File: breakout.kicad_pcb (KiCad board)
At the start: 2 copper layers, 103 x 62 mm, 32 parts, among them CON1 SD_Card, CON2 USB-MICRO-AB, P2 CONN_01X40, P3 CONN_01X40, P4 CONN_01X40, P5 A-DF-09-A/KG-T4S, SW1 SW_PUSH

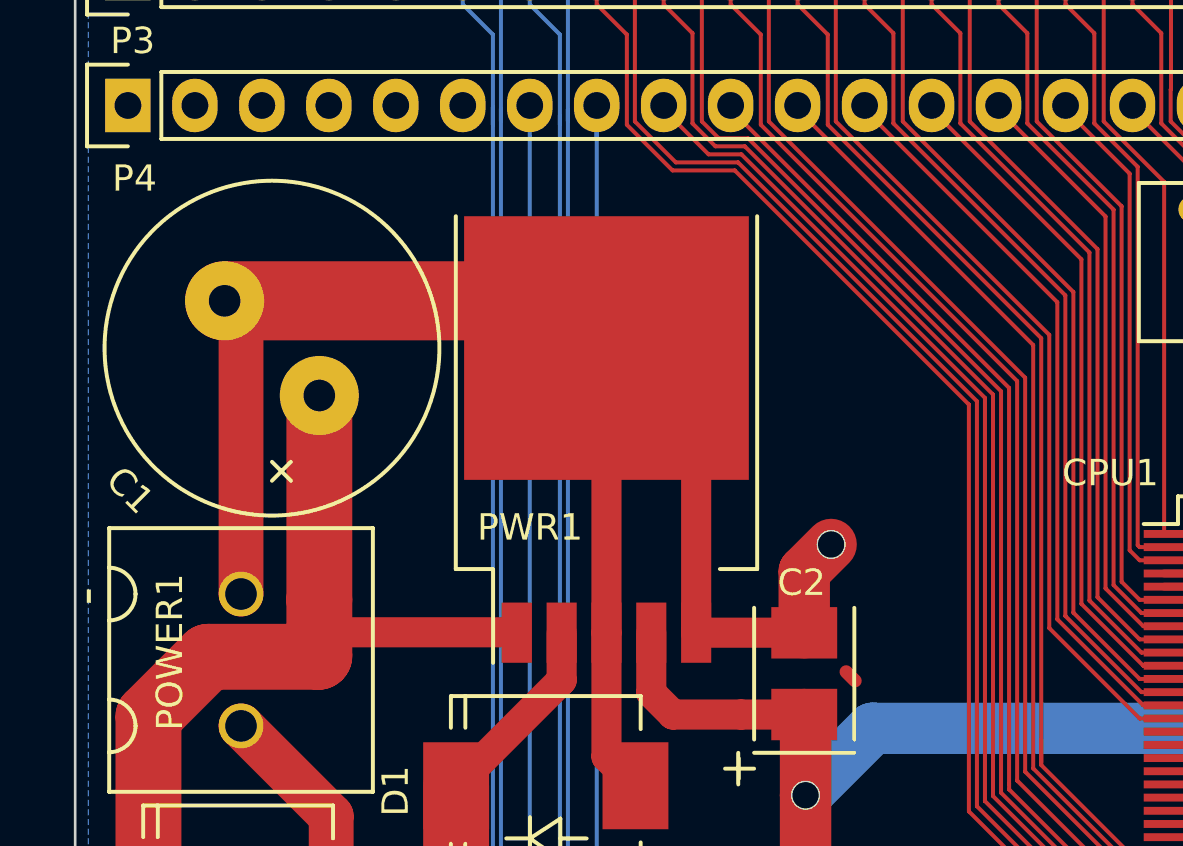
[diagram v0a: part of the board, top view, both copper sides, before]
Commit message: added thermal sink for 3.3reg
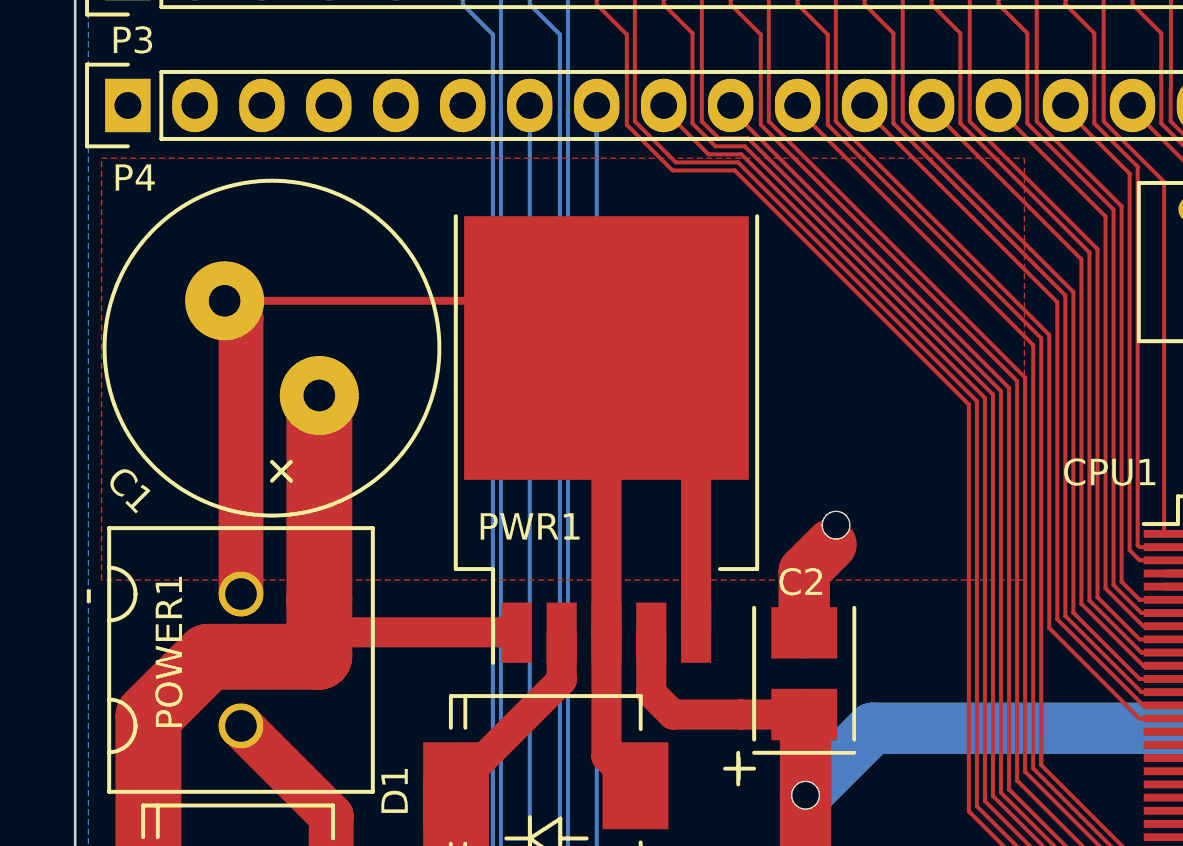
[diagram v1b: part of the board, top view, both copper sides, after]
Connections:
- P2 pad 25: (no net) -> GND
- P2 pad 26: (no net) -> GND
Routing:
- net GND: track 143.9 -> 139.8 mm

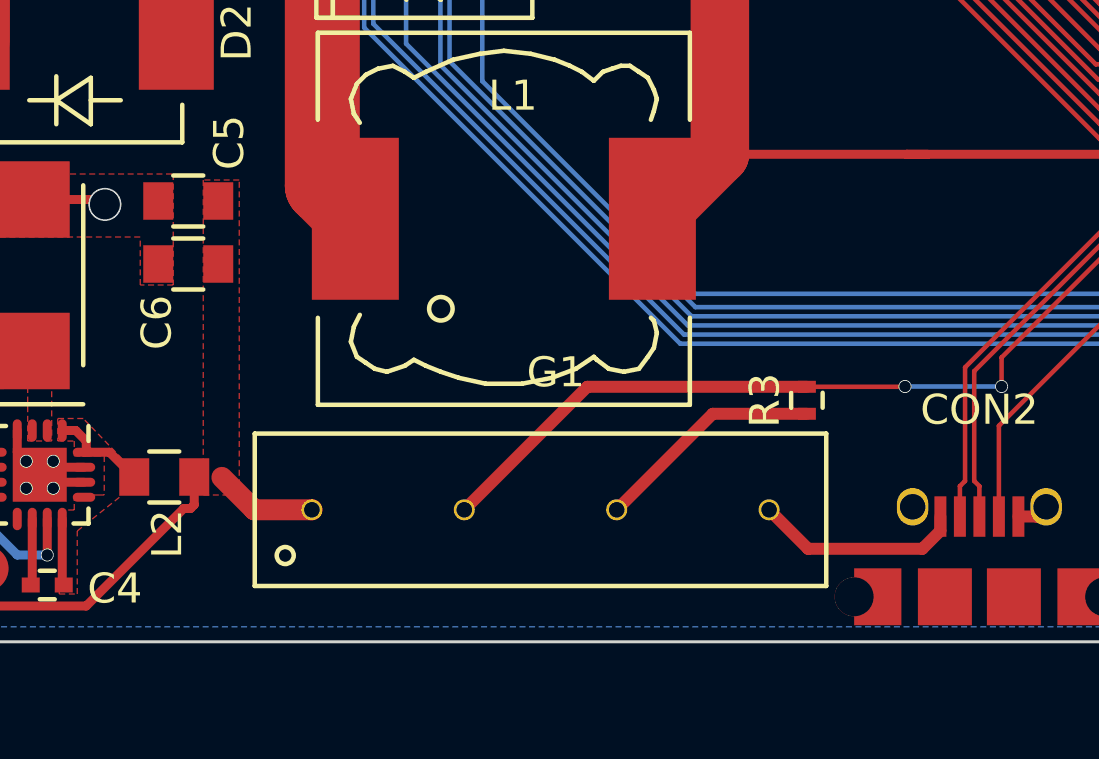
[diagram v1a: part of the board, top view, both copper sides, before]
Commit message: improved 5V FET and added to schematic & board
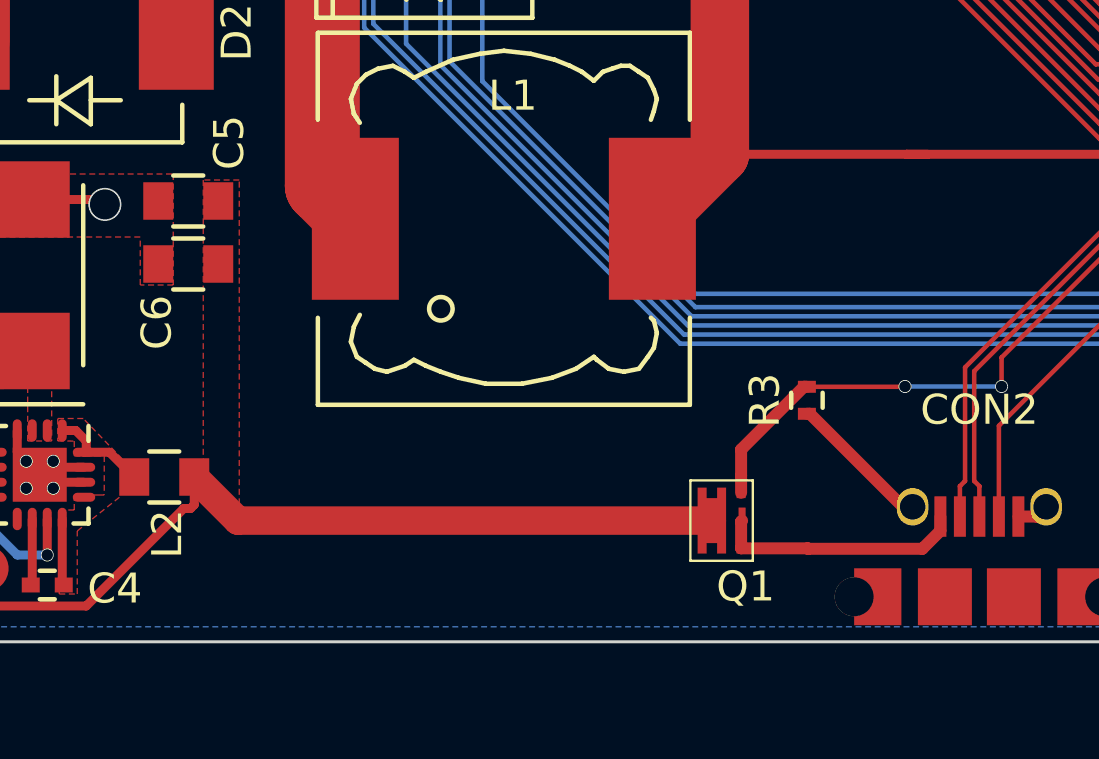
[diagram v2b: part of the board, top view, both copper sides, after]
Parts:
- removed G1: 9007-05-00, Custom Footprints:9007-05-00
- added Q1: SIA461DJ-T1-GE3, Custom Footprints:PowerPak_SC-70-6L-Single, F.Cu at (85.8, 171.0)
- CON1: footprint SD_MMC_Card_Receptacle -> Custom Footprints:SD_MMC_Card_Receptacle
- CON2: footprint USB_MICRO_AB -> Custom Footprints:USB_MICRO_AB
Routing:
- net /5V: track 19.8 -> 34.2 mm
- net /USB0_PPWR: track 36.9 -> 28.3 mm
- net GND: track 139.8 -> 136.9 mm
- net Net-(CON2-Pad1): track 6.97 -> 8.31 mm

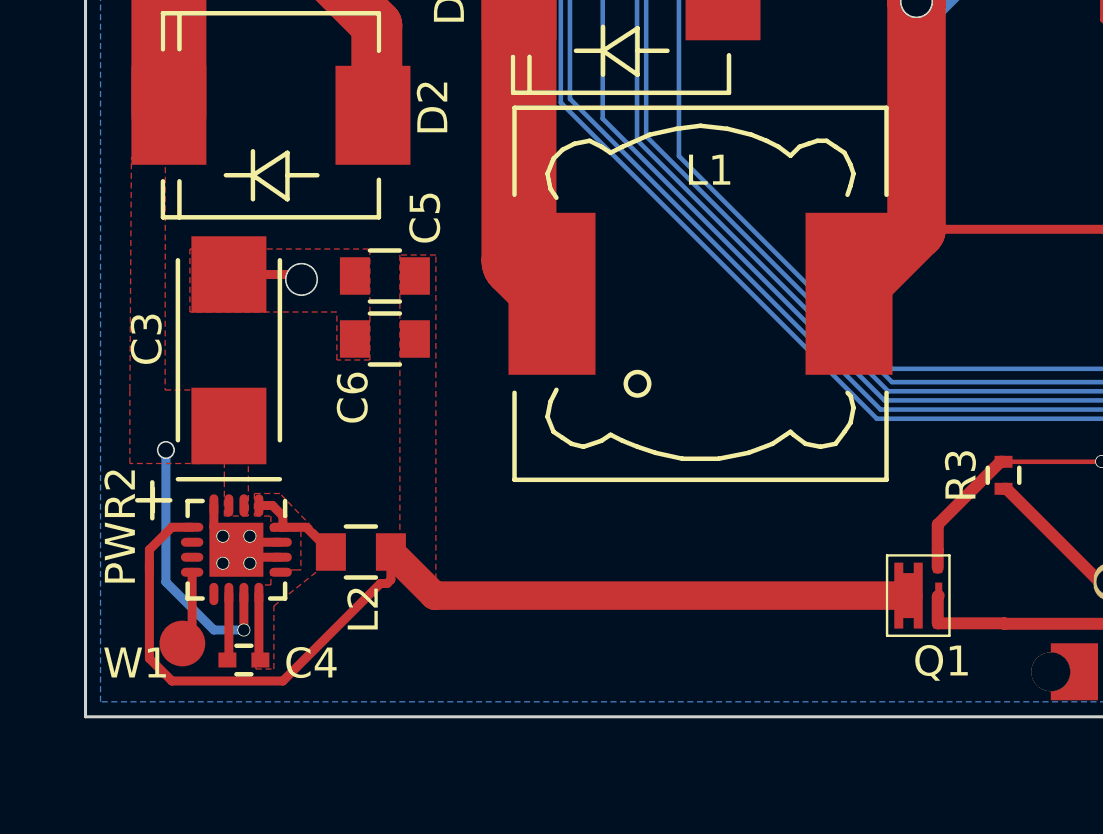
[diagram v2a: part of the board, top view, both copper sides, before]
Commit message: routed 5V FET
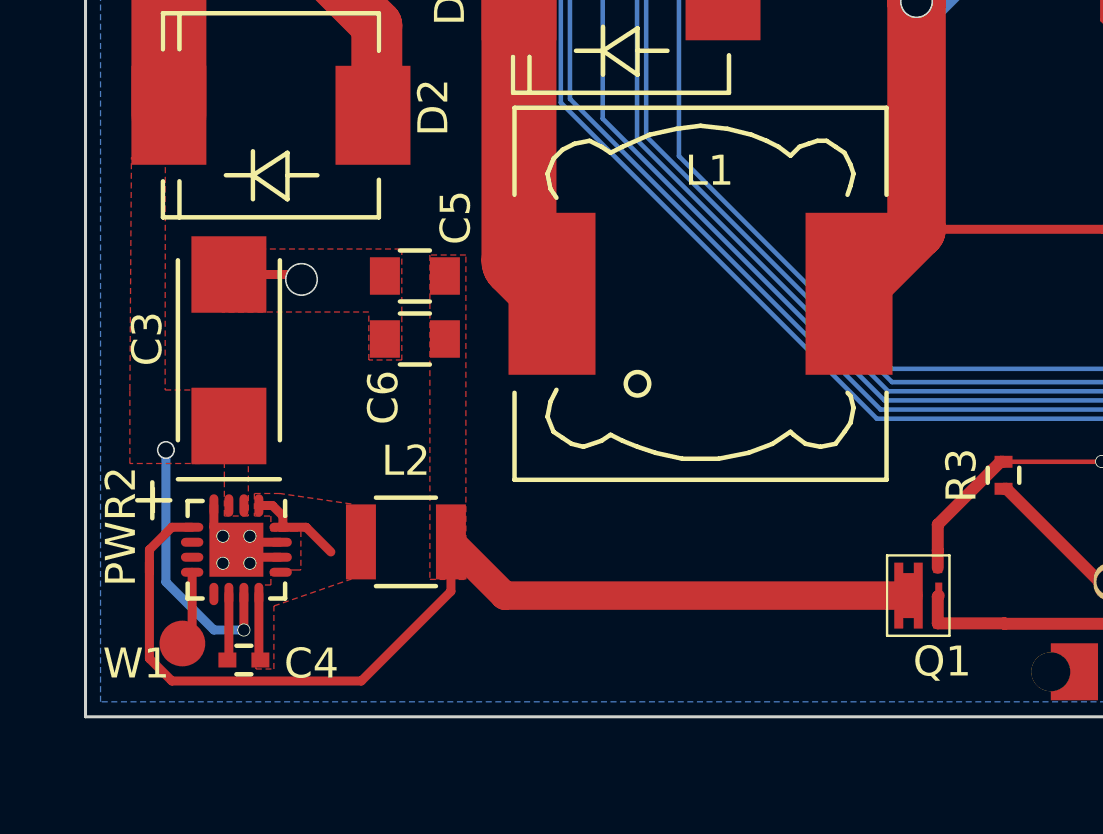
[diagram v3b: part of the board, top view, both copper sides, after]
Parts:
- L2: footprint Capacitors_SMD:C_0805 -> Capacitors_SMD:C_1210
- moved L2 1.54 mm to (68.7, 169.2)
- moved C5 1.00 mm to (69.0, 160.3)
- moved C6 1.00 mm to (69.0, 162.4)
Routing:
- net /5V: track 34.2 -> 34.9 mm
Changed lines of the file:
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@@
   (general
     (links 229)
-    (no_connects 22)
+    (no_connects 50)
     (area 57.949999 112.949999 161.050001 175.050001)
     (thickness 1.6)
     (drawings 11)
-    (tracks 1089)
+    (tracks 1087)
     (zones 0)
     (modules 32)
@@
       (net 1 GND))
   )
-  (module Capacitors_SMD:C_0805 locked (layer F.Cu)
-    (at 67.1787 169.50688)
-    (descr "Capacitor SMD 0805, reflow soldering, AVX (see smccp.pdf)")
-    (tags "capacitor 0805")
-    (attr smd)
-    (fp_text reference L2 (at 0.1 1.9 90) (layer F.SilkS)
-      (effects (font (size 1 1) (thickness 0.15)))
-    )
-    (fp_text value 4.7uH (at 0 2.1) (layer F.Fab)
-      (effects (font (size 1 1) (thickness 0.15)))
-    )
-    (fp_line (start -1.8 -1) (end 1.8 -1) (layer F.CrtYd) (width 0.05))
-    (fp_line (start -1.8 1) (end 1.8 1) (layer F.CrtYd) (width 0.05))
-    (fp_line (start -1.8 -1) (end -1.8 1) (layer F.CrtYd) (width 0.05))
-    (fp_line (start 1.8 -1) (end 1.8 1) (layer F.CrtYd) (width 0.05))
-    (fp_line (start 0.5 -0.85) (end -0.5 -0.85) (layer F.SilkS) (width 0.15))
-    (fp_line (start -0.5 0.85) (end 0.5 0.85) (layer F.SilkS) (width 0.15))
-    (pad 1 smd rect (at -1 0) (size 1 1.25) (layers F.Cu F.Paste F.Mask)
-      (net 16 /VSW))
-    (pad 2 smd rect (at 1 0) (size 1 1.25) (layers F.Cu F.Paste F.Mask)
-      (net 17 /5V))
-    (model Capacitors_SMD.3dshapes/C_0805.wrl
-      (at (xyz 0 0 0))
-      (scale (xyz 1 1 1))
-      (rotate (xyz 0 0 0))
-    )
-  )
   (module "Custom Footprints:DIN9F" locked (layer F.Cu)
     (at 125 171 180)
@@
   )
   (module Capacitors_SMD:C_0805 locked (layer F.Cu)
-    (at 67.9787 160.30688 180)
+    (at 68.9787 160.30688 180)
     (descr "Capacitor SMD 0805, reflow soldering, AVX (see smccp.pdf)")
     (tags "capacitor 0805")
@@
   )
   (module Capacitors_SMD:C_0805 locked (layer F.Cu)
-    (at 67.9787 162.40688 180)
+    (at 68.9787 162.40688 180)
     (descr "Capacitor SMD 0805, reflow soldering, AVX (see smccp.pdf)")
     (tags "capacitor 0805")
@@
       (net 2 "Net-(CON2-Pad1)"))
   )
+  (module Capacitors_SMD:C_1210 (layer F.Cu)
+    (at 68.68 169.17)
+    (descr "Capacitor SMD 1210, reflow soldering, AVX (see smccp.pdf)")
+    (tags "capacitor 1210")
+    (attr smd)
+    (fp_text reference L2 (at 0 -2.7) (layer F.SilkS)
+      (effects (font (size 1 1) (thickness 0.15)))
+    )
+    (fp_text value 4.7uH (at 0 2.7) (layer F.Fab)
+      (effects (font (size 1 1) (thickness 0.15)))
+    )
+    (fp_line (start -2.3 -1.6) (end 2.3 -1.6) (layer F.CrtYd) (width 0.05))
+    (fp_line (start -2.3 1.6) (end 2.3 1.6) (layer F.CrtYd) (width 0.05))
+    (fp_line (start -2.3 -1.6) (end -2.3 1.6) (layer F.CrtYd) (width 0.05))
+    (fp_line (start 2.3 -1.6) (end 2.3 1.6) (layer F.CrtYd) (width 0.05))
+    (fp_line (start 1 -1.475) (end -1 -1.475) (layer F.SilkS) (width 0.15))
+    (fp_line (start -1 1.475) (end 1 1.475) (layer F.SilkS) (width 0.15))
+    (pad 1 smd rect (at -1.5 0) (size 1 2.5) (layers F.Cu F.Paste F.Mask)
+      (net 16 /VSW))
+    (pad 2 smd rect (at 1.5 0) (size 1 2.5) (layers F.Cu F.Paste F.Mask)
+      (net 17 /5V))
+    (model Capacitors_SMD.3dshapes/C_1210.wrl
+      (at (xyz 0 0 0))
+      (scale (xyz 1 1 1))
+      (rotate (xyz 0 0 0))
+    )
+  )
   (gr_text - (at 58.64 143.61 270) (layer F.SilkS)
     (effects (font (size 1.4 1.4) (thickness 0.28)))
@@
   (segment (start 66.1787 169.50688) (end 65.3537 168.68188) (width 0.3) (layer F.Cu) (net 16))
   (segment (start 65.3537 168.68188) (end 64.5037 168.68188) (width 0.3) (layer F.Cu) (net 16))
-  (segment (start 85.4325 170.96) (end 69.63182 170.96) (width 0.95) (layer F.Cu) (net 17))
-  (segment (start 69.63182 170.96) (end 68.1787 169.50688) (width 0.95) (layer F.Cu) (net 17))
-  (segment (start 60.1287 169.849839) (end 60.1287 170.179964) (width 0.3) (layer F.Cu) (net 17))
+  (segment (start 85.4325 170.96) (end 71.97 170.96) (width 0.95) (layer F.Cu) (net 17))
+  (segment (start 71.97 170.96) (end 70.18 169.17) (width 0.95) (layer F.Cu) (net 17))
   (segment (start 60.1287 170.179964) (end 60.1287 173.05688) (width 0.3) (layer F.Cu) (net 17))
+  (segment (start 60.1287 173.05688) (end 60.8787 173.80688) (width 0.3) (layer F.Cu) (net 17))
+  (segment (start 60.8787 173.80688) (end 67.19312 173.80688) (width 0.3) (layer F.Cu) (net 17))
+  (segment (start 67.19312 173.80688) (end 70.18 170.82) (width 0.3) (layer F.Cu) (net 17))
+  (segment (start 70.18 170.82) (end 70.18 169.17) (width 0.3) (layer F.Cu) (net 17))
+  (segment (start 60.1287 169.849839) (end 60.1287 170.179964) (width 0.3) (layer F.Cu) (net 17))
   (segment (start 61.5537 168.68188) (end 60.8787 168.68188) (width 0.3) (layer F.Cu) (net 17))
   (segment (start 60.8787 168.68188) (end 60.1287 169.43188) (width 0.3) (layer F.Cu) (net 17))
   (segment (start 60.1287 169.43188) (end 60.1287 170.179964) (width 0.3) (layer F.Cu) (net 17))
-  (segment (start 67.8287 170.55688) (end 68.0537 170.55688) (width 0.3) (layer F.Cu) (net 17))
-  (segment (start 68.0537 170.55688) (end 68.1787 170.43188) (width 0.3) (layer F.Cu) (net 17))
-  (segment (start 68.1787 170.43188) (end 68.1787 169.50688) (width 0.3) (layer F.Cu) (net 17))
-  (segment (start 64.5787 173.80688) (end 67.8287 170.55688) (width 0.3) (layer F.Cu) (net 17))
-  (segment (start 60.8787 173.80688) (end 64.5787 173.80688) (width 0.3) (layer F.Cu) (net 17))
-  (segment (start 60.1287 173.05688) (end 60.8787 173.80688) (width 0.3) (layer F.Cu) (net 17))
   (segment (start 88.6 166.5) (end 88.5 166.5) (width 0.4) (layer F.Cu) (net 18))
   (segment (start 88.5 166.5) (end 86.4075 168.5925) (width 0.4) (layer F.Cu) (net 18))
@@
     (polygon
       (pts
-        (xy 61.4787 161.50688) (xy 61.4787 159.40688) (xy 67.4787 159.40688) (xy 67.4787 163.10688) (xy 66.3787 163.10688)
-        (xy 66.3787 161.50688)
+        (xy 62.542901 161.50688) (xy 62.542901 159.40688) (xy 68.542901 159.40688) (xy 68.542901 163.10688) (xy 67.442901 163.10688)
+        (xy 67.442901 161.50688)
       )
     )
@@
       (pts
         (xy 63.6787 170.70688) (xy 63.6787 173.40688) (xy 64.2787 173.40688) (xy 64.2787 171.30688) (xy 64.2787 171.30688)
-        (xy 65.7787 170.10688) (xy 65.7787 168.90688) (xy 64.4787 167.55688) (xy 63.6287 167.55688) (xy 63.6287 168.30688)
+        (xy 66.86 170.41) (xy 66.86 167.90686) (xy 64.4787 167.55688) (xy 63.6287 167.55688) (xy 63.6287 168.30688)
         (xy 64.1787 168.308663) (xy 64.1787 168.80688) (xy 64.8787 168.80688) (xy 65.1787 168.80688) (xy 65.1787 170.10688)
         (xy 64.9787 170.10688) (xy 64.1787 170.10688) (xy 64.1787 170.40688) (xy 64.1787 170.60688) (xy 63.6787 170.60688)
@@
     (polygon
       (pts
-        (xy 68.4787 159.60688) (xy 68.4787 170.42) (xy 69.6787 170.42) (xy 69.6787 159.60688)
+        (xy 69.4787 159.60688) (xy 69.4787 170.42) (xy 70.6787 170.42) (xy 70.6787 159.60688)
       )
     )
